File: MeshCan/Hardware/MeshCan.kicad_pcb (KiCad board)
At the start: 4 copper layers, 16 parts, among them IC1 ATMEGA2564/1284/644RFR2, P1 CONN34

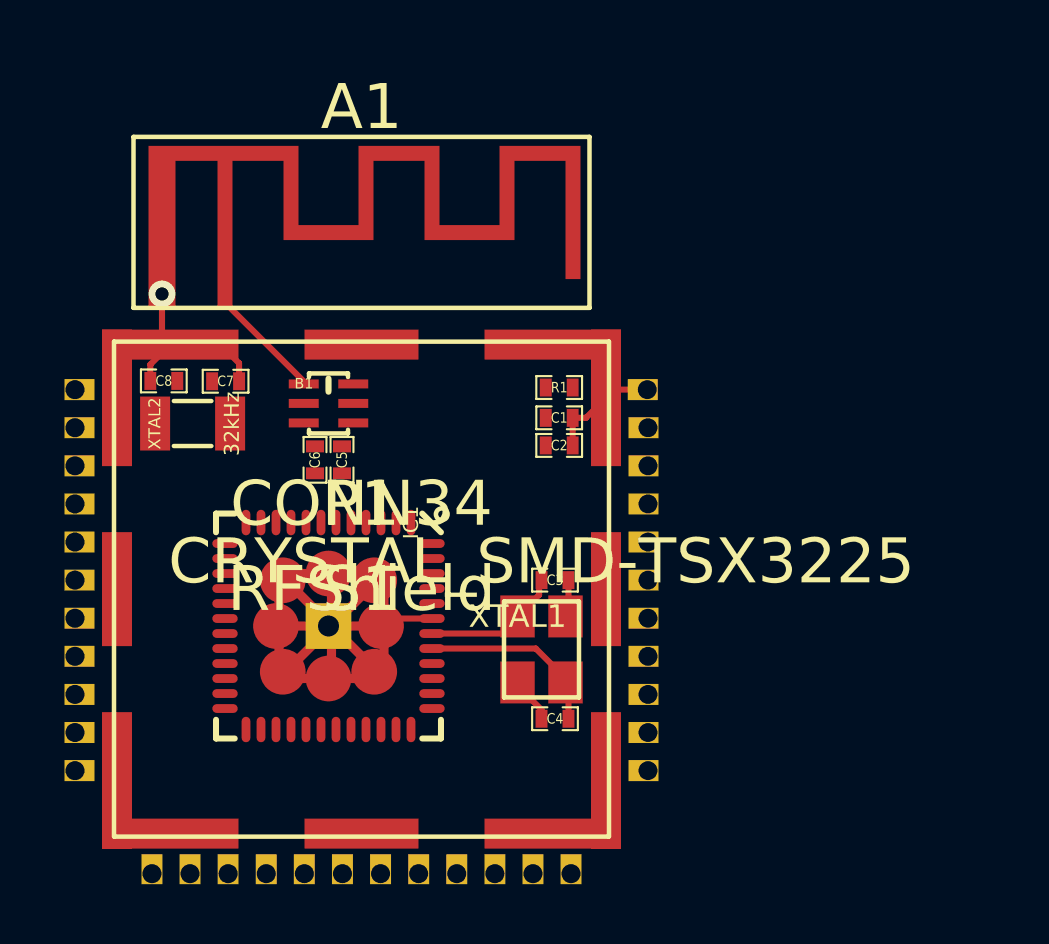
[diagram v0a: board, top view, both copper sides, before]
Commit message: Import traces, minor movements, .gitignore.
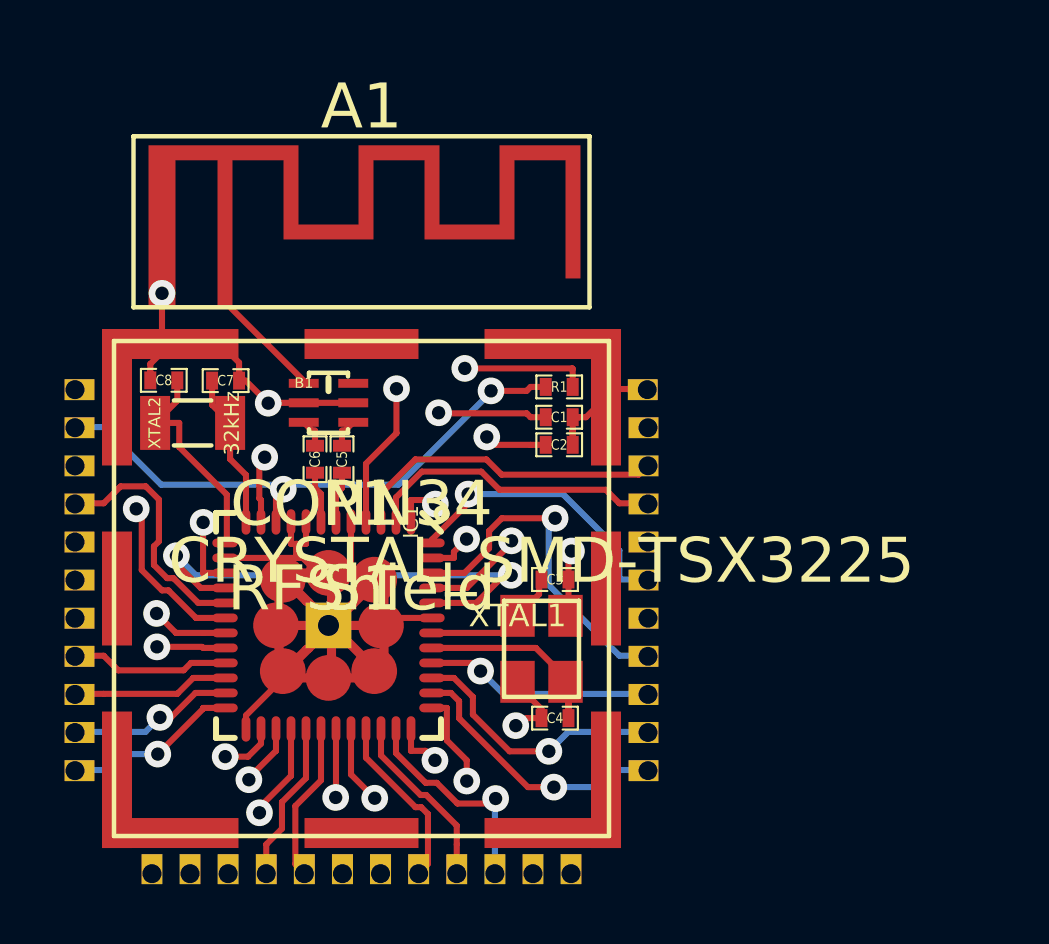
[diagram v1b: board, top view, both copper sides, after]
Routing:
- net +3.3V: track 0.00 -> 43.8 mm, vias 0 -> 3
- net GND: track 43.2 -> 65.3 mm, vias 1 -> 4
- net Reset: track 0.00 -> 19.2 mm, vias 0 -> 2
- net Net-(C1-Pad1): track 0.00 -> 15.5 mm, vias 0 -> 2
- net PF7: track 0.00 -> 13.8 mm, vias 0 -> 1
- net Net-(C2-Pad1): track 0.00 -> 13.6 mm, vias 0 -> 2
- net PF0: track 0.00 -> 11.8 mm, vias 0 -> 1
- net PF6: track 0.00 -> 10.7 mm
- net PF5: track 0.00 -> 10.0 mm
- net PF2: track 0.00 -> 9.87 mm, vias 0 -> 1
- net PF3-4: track 0.00 -> 9.78 mm, vias 0 -> 1
- net PF1: track 0.00 -> 9.59 mm, vias 0 -> 1
- net PE4: track 0.00 -> 9.07 mm, vias 0 -> 1
- net PE5: track 0.00 -> 8.83 mm, vias 0 -> 1
- net PE3: track 0.00 -> 8.74 mm, vias 0 -> 1
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
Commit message: GND/PWR planes. Trace cleanup and anchor traces to TH pads.
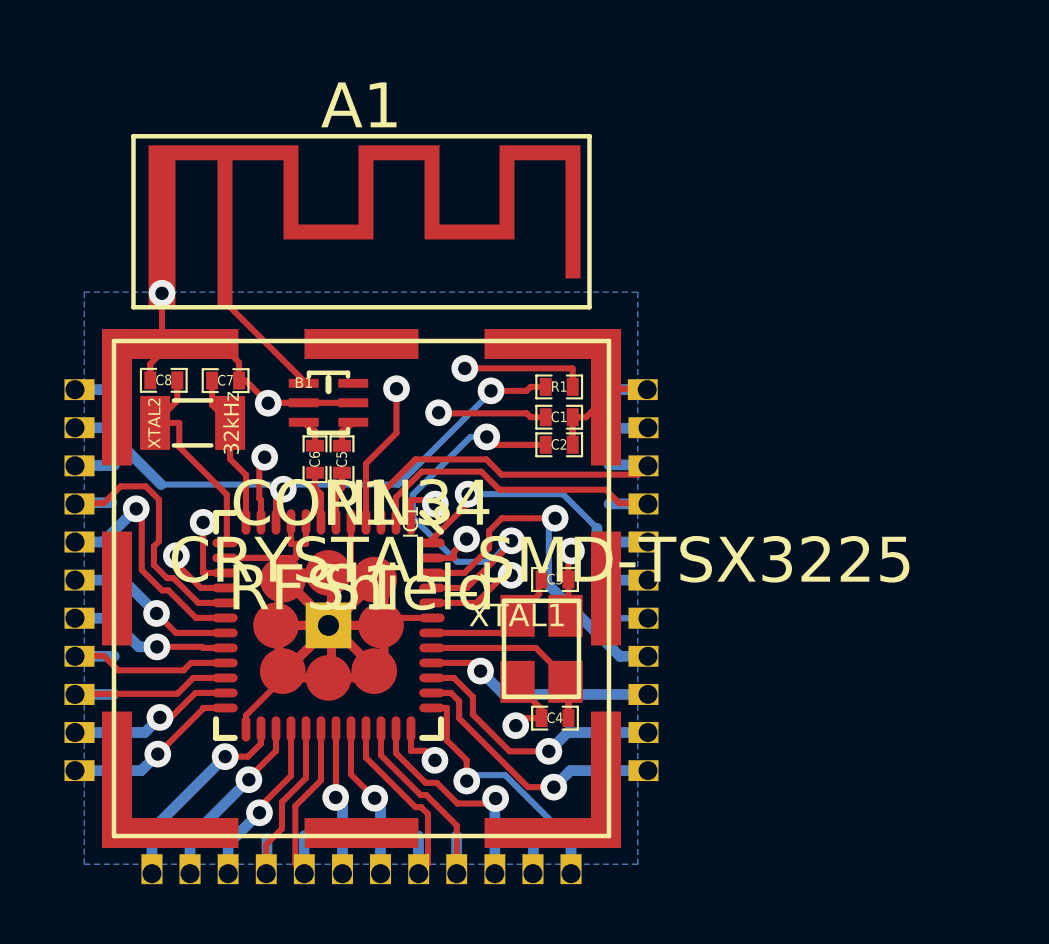
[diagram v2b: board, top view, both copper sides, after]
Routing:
- net PE7: track 7.63 -> 13.5 mm
- net PF0: track 11.8 -> 16.1 mm
- net Reset: track 19.2 -> 22.9 mm
- net PE5: track 8.83 -> 12.4 mm
- net PD6: track 5.54 -> 8.58 mm
- net PF7: track 13.8 -> 16.7 mm
- net GND: track 65.3 -> 68.2 mm
- net PF1: track 9.59 -> 12.3 mm
- net TX0: track 7.39 -> 9.87 mm
- net PB6: track 5.21 -> 7.55 mm
- net PB5: track 4.90 -> 7.24 mm
- net PG1: track 8.69 -> 11.0 mm
- net PE2: track 7.45 -> 9.67 mm
- net PF3-4: track 9.78 -> 11.8 mm
- net MOSI: track 5.67 -> 7.67 mm
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- added copper zone on Inner1.Cu, net +3.3V
- added copper zone on B.Cu, net GND

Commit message: Approaching layout finish. Transitioning to meshthing repo.
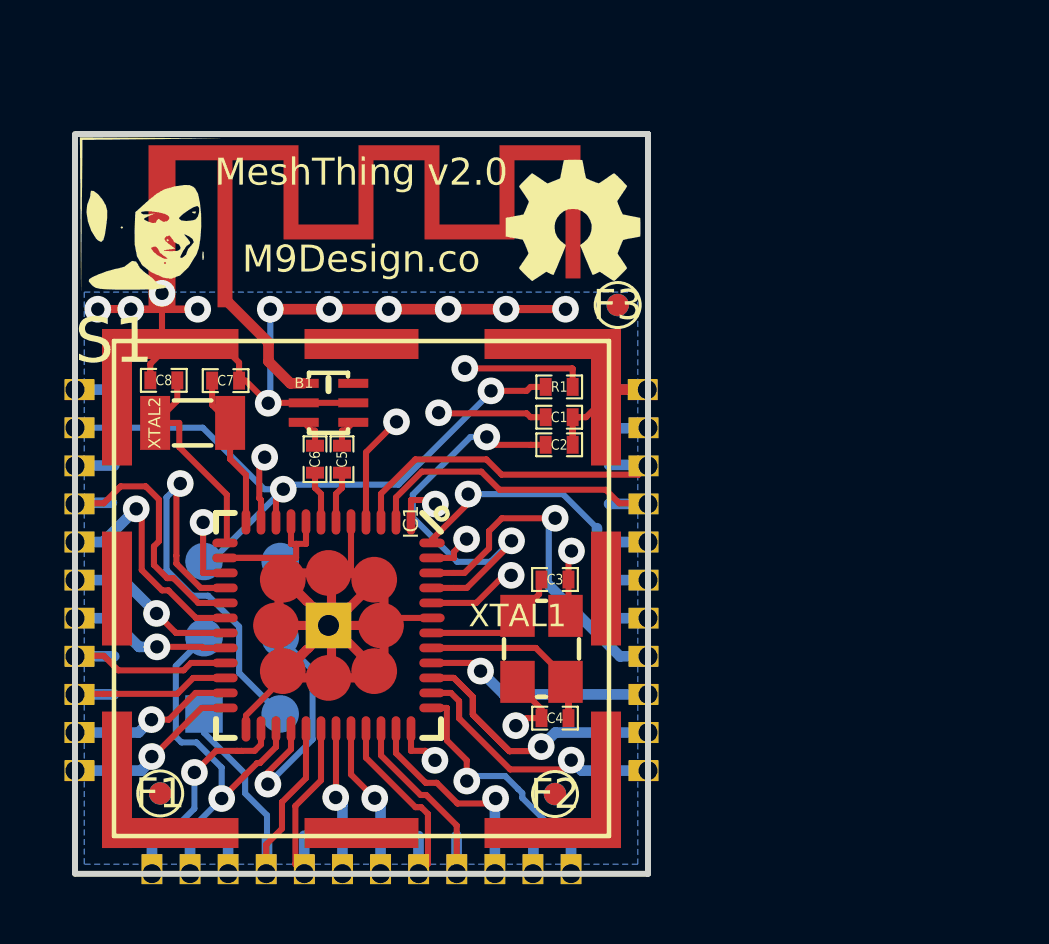
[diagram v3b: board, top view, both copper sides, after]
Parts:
- added F1: CONN_1, _MT_MC_Pretty:_MT_Fiducial, F.Cu at (143.3, 109.7)
- added F2: CONN_1, _MT_MC_Pretty:_MT_Fiducial, F.Cu at (156.4, 109.7)
- added F3: CONN_1, _MT_MC_Pretty:_MT_Fiducial, F.Cu at (158.5, 93.4)
- added G***: LOGO, _MT_OHW_LOGO:LOGO, F.Cu at (157.1, 90.5)
- added H1: ICSP, _MT_MC_Pretty:_MC_pin_pad_3x2, B.Cu at (146.0, 104.5)
- added PrettyLady: PrettyLady, _MT_MC_Pretty:_MC_LOGO-PrettyLady, F.Cu at (142.9, 90.3)
- XTAL2: footprint _MT_TF32D-32768-Crystal -> _MT_MC_Pretty:_MC_TF32D-32768-Crystal
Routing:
- net GND: track 68.2 -> 94.8 mm, vias 4 -> 13
- net +3.3V: track 45.2 -> 59.2 mm
- net SCK: track 7.18 -> 15.1 mm
- net MOSI: track 7.67 -> 14.6 mm
- net MISO: track 6.53 -> 11.6 mm
- net PD7: track 5.88 -> 8.85 mm
- net PD6: track 8.58 -> 6.16 mm
- net PB0/SS: track 8.24 -> 10.4 mm
- net PF1: track 12.3 -> 13.6 mm
- net PE5: track 12.4 -> 13.4 mm
- net PF7: track 16.7 -> 16.0 mm
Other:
- board outline added: 19.1 x 24.7 mm
- board text added: "MeshThing v2.0 M9Design.co"
- board text added: "MeshThing v2.0 © M9Design.co 2013 Designed by Robert Powers"
- board text added: "OpenHardware Under TAPR OHL tapr.org/OHL"
